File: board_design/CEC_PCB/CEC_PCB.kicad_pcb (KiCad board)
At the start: 4 copper layers, 4 parts, among them J1 HDMI_A, J2 HDMI_A, J3 Conn_01x12_Socket, J4 Conn_01x12_Socket

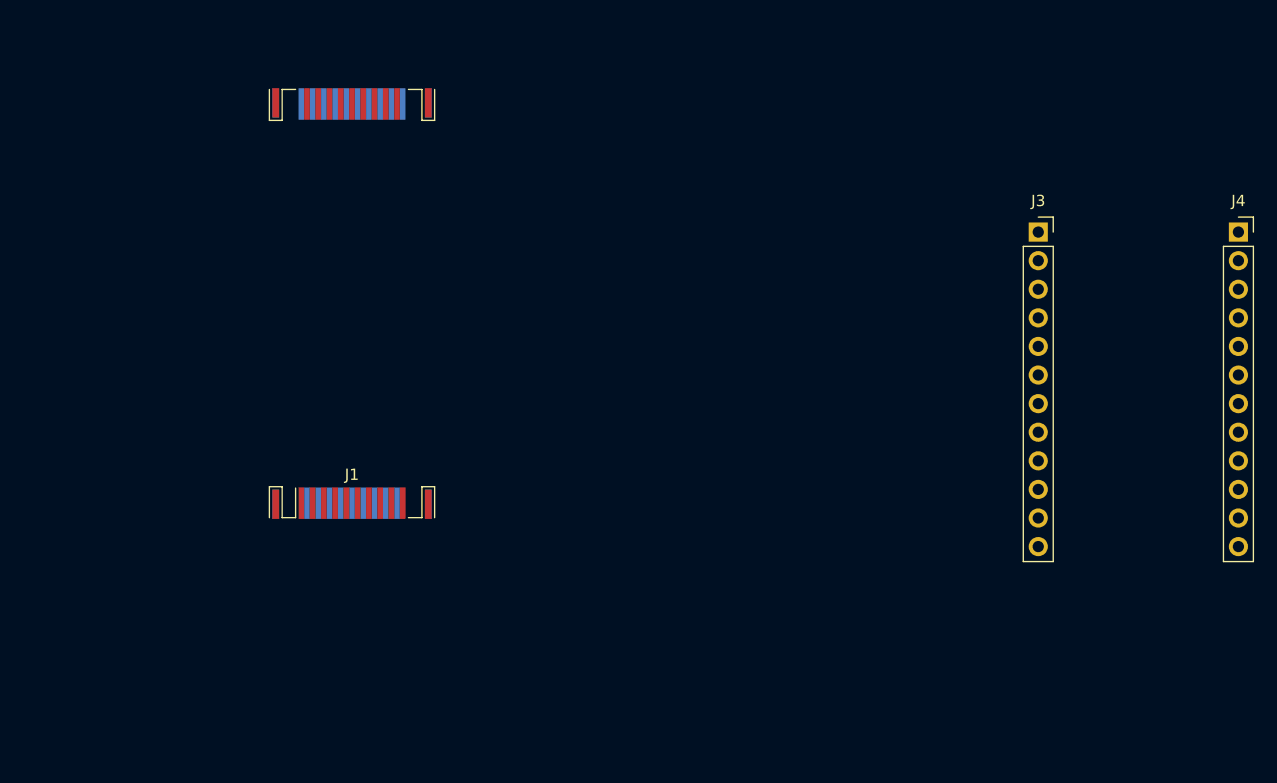
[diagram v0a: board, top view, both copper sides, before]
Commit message: Broke out Pro Micro pins using a connector with two rows Level shifter between CEC pins Mounting holes and debug pins PCB outline defined Crude component placement Copper pours on GND planes
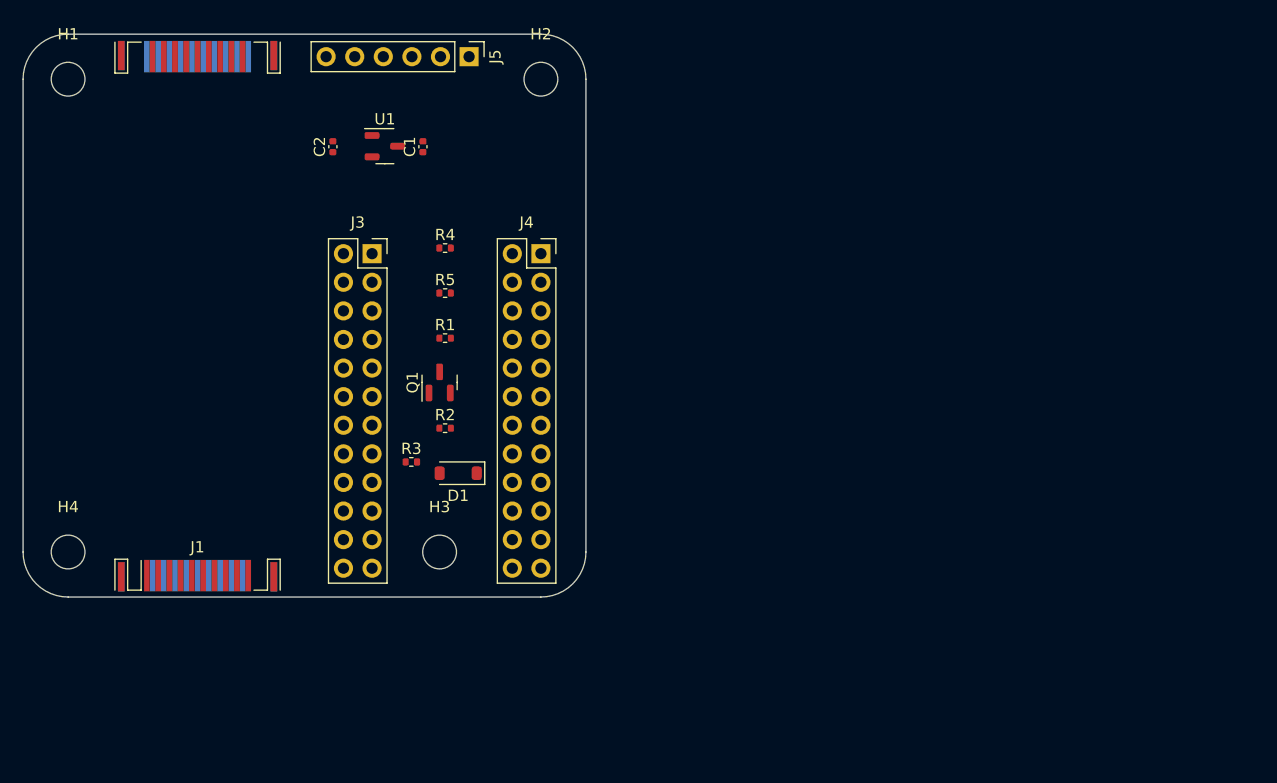
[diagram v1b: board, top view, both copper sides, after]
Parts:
- added C1: 0.1u, Capacitor_SMD:C_0402_1005Metric, F.Cu at (115.5, 61.0)
- added C2: 0.1u, Capacitor_SMD:C_0402_1005Metric, F.Cu at (107.5, 61.0)
- added D1: 1N4148W, Diode_SMD:D_SOD-123, F.Cu at (118.7, 90.0)
- added H1: MountingHole, MountingHole:MountingHole_3mm, F.Cu at (84.0, 55.0)
- added H2: MountingHole, MountingHole:MountingHole_3mm, F.Cu at (126.0, 55.0)
- added H3: MountingHole, MountingHole:MountingHole_3mm, F.Cu at (117.0, 97.0)
- added H4: MountingHole, MountingHole:MountingHole_3mm, F.Cu at (84.0, 97.0)
- added J5: Conn_01x06_Pin, Connector_PinHeader_2.54mm:PinHeader_1x06_P2.54mm_Vertical, F.Cu at (119.6, 53.0)
- added Q1: BSS138, Package_TO_SOT_SMD:SOT-23, F.Cu at (117.0, 81.9)
- added R1: 10k, Resistor_SMD:R_0402_1005Metric, F.Cu at (117.5, 78.0)
- added R2: 10k, Resistor_SMD:R_0402_1005Metric, F.Cu at (117.5, 86.0)
- added R3: 27k, Resistor_SMD:R_0402_1005Metric, F.Cu at (114.5, 89.0)
- added R4: 2k2, Resistor_SMD:R_0402_1005Metric, F.Cu at (117.5, 70.0)
- added R5: 2k2, Resistor_SMD:R_0402_1005Metric, F.Cu at (117.5, 74.0)
- added U1: XC6206PxxxMR, Package_TO_SOT_SMD:SOT-23-3, F.Cu at (112.1, 61.0)
- J3, J4: value Conn_01x12_Socket -> Conn_02x12_Odd_Even; footprint Connector_PinSocket_2.54mm:PinSocket_1x12_P2.54mm_Vertical -> Connector_PinSocket_2.54mm:PinSocket_2x12_P2.54mm_Vertical
- moved J4 62.0 mm to (126.0, 70.5)
- moved J3 59.2 mm to (111.0, 70.5)
- moved J1 15.2 mm to (95.5, 99.1)
- moved J2 14.3 mm to (95.5, 53.0)
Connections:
- J3 pad 1: unconnected-(J3-Pin_1-Pad1) -> /TX
- J3 pad 10: unconnected-(J3-Pin_10-Pad10) -> /SDA
- J3 pad 11: unconnected-(J3-Pin_11-Pad11) -> /SCL
- J3 pad 12: unconnected-(J3-Pin_12-Pad12) -> /SCL
- J3 pad 2: unconnected-(J3-Pin_2-Pad2) -> /TX
- J3 pad 3: unconnected-(J3-Pin_3-Pad3) -> /RX
- J3 pad 4: unconnected-(J3-Pin_4-Pad4) -> /RX
- J3 pad 5: unconnected-(J3-Pin_5-Pad5) -> Net-(J3-Pin_5)
- J3 pad 6: unconnected-(J3-Pin_6-Pad6) -> Net-(J3-Pin_5)
- J3 pad 7: unconnected-(J3-Pin_7-Pad7) -> Net-(J3-Pin_7)
- J3 pad 8: unconnected-(J3-Pin_8-Pad8) -> Net-(J3-Pin_7)
- J3 pad 9: unconnected-(J3-Pin_9-Pad9) -> /SDA
- J4 pad 1: unconnected-(J4-Pin_1-Pad1) -> Net-(J4-Pin_1)
- J4 pad 10: unconnected-(J4-Pin_10-Pad10) -> Net-(J4-Pin_10)
- J4 pad 11: unconnected-(J4-Pin_11-Pad11) -> Net-(J4-Pin_11)
- J4 pad 12: unconnected-(J4-Pin_12-Pad12) -> Net-(J4-Pin_11)
- J4 pad 2: unconnected-(J4-Pin_2-Pad2) -> Net-(J4-Pin_1)
- J4 pad 3: unconnected-(J4-Pin_3-Pad3) -> GND
- J4 pad 4: unconnected-(J4-Pin_4-Pad4) -> GND
- J4 pad 5: unconnected-(J4-Pin_5-Pad5) -> Net-(J4-Pin_5)
- J4 pad 6: unconnected-(J4-Pin_6-Pad6) -> Net-(J4-Pin_5)
- J4 pad 7: unconnected-(J4-Pin_7-Pad7) -> VCC
- J4 pad 8: unconnected-(J4-Pin_8-Pad8) -> VCC
- J4 pad 9: unconnected-(J4-Pin_9-Pad9) -> Net-(J4-Pin_10)
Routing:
- added copper zone on In1.Cu, net GND
- added copper zone on In2.Cu, net GND
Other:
- board outline added: 50 x 50 mm

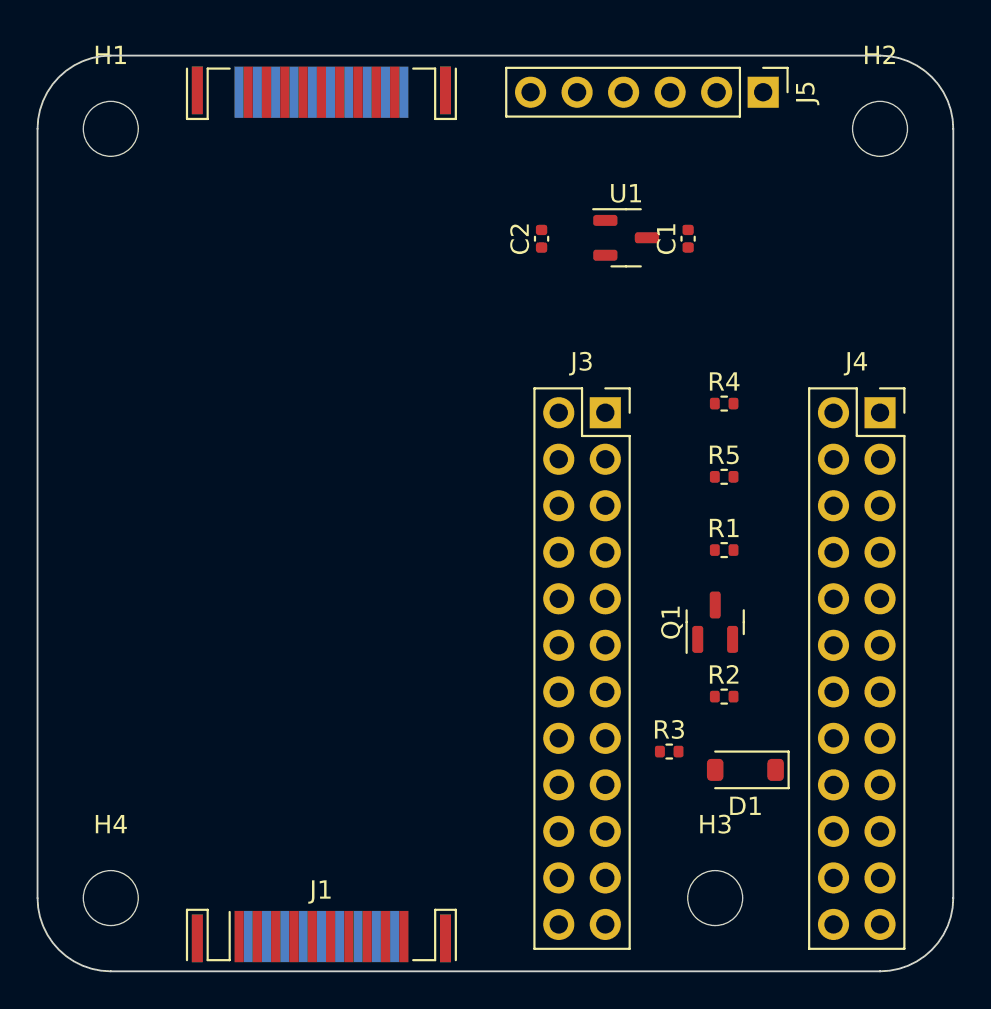
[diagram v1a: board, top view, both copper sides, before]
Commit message: Labels for nets in the schematic Board size change Parts placement change Basic routing
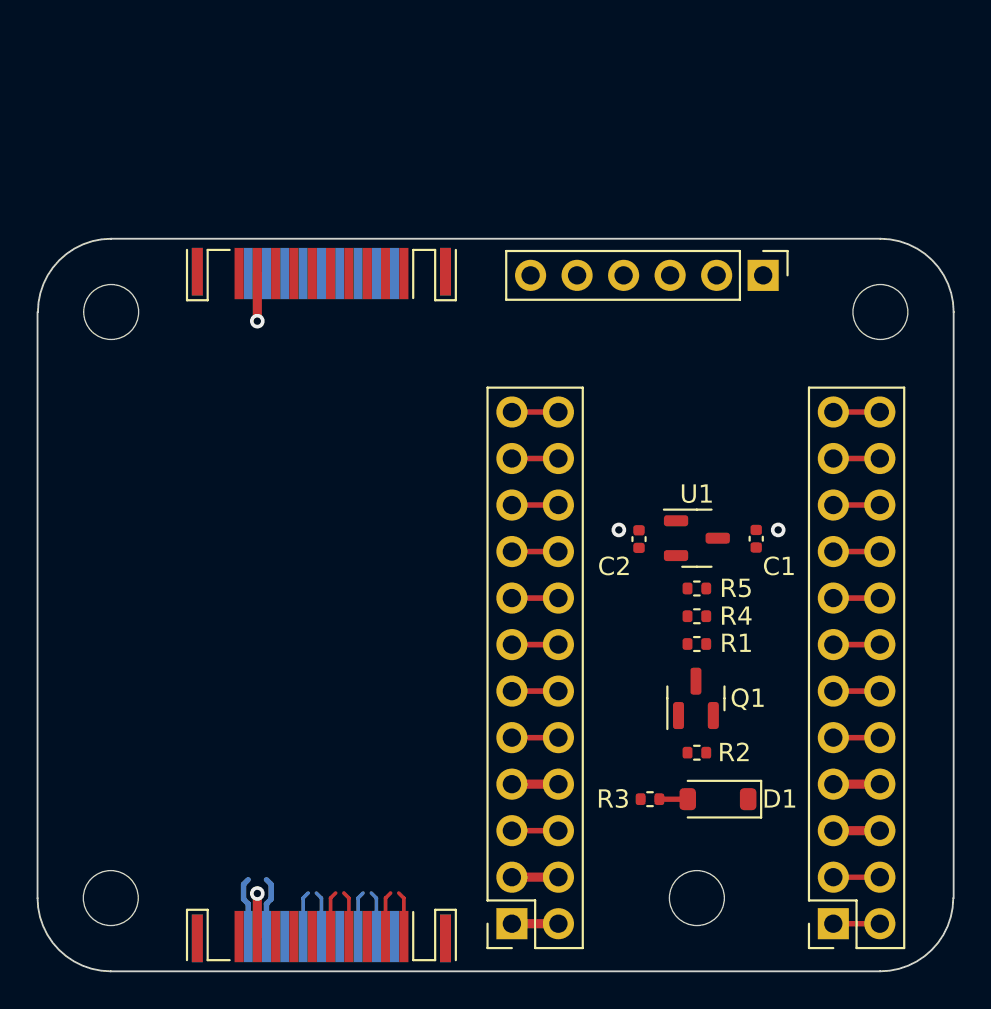
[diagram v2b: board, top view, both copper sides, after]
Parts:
- J2: moved to F.Cu
- moved J4 34.4 mm to (105.9, 98.4), turned to 180 degrees
- moved J3 30.6 mm to (123.5, 98.4), turned to 180 degrees
- moved C2 17.2 mm to (112.8, 77.4)
- moved U1 16.8 mm to (116.0, 77.3)
- moved C1 16.8 mm to (119.2, 77.4)
- moved R4 11.7 mm to (116.0, 81.6), turned to 180 degrees
- moved H1 10.0 mm to (84.0, 65.0)
- moved H2 10.0 mm to (126.0, 65.0)
- moved J5 10.0 mm to (119.6, 63.0)
- moved J2 9.90 mm to (95.5, 62.9), turned to 180 degrees
- moved R5 6.28 mm to (116.0, 80.1), turned to 180 degrees
- moved R1 5.34 mm to (116.0, 83.1)
- moved Q1 4.29 mm to (115.9, 86.1)
- moved R2 3.41 mm to (116.0, 89.1)
- moved R3 2.80 mm to (113.4, 91.6)
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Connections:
- net Net-(D1-A) renamed /D_K
- net Net-(J1-+5V) renamed /+5V
- net Net-(J1-CK+) renamed /CK+
- net Net-(J1-CK-) renamed /CK-
- net Net-(J1-D0+) renamed /D0+
- net Net-(J1-D0-) renamed /D0-
- net Net-(J1-D1+) renamed /D1+
- net Net-(J1-D1-) renamed /D1-
- net Net-(J1-D2+) renamed /D2+
- net Net-(J1-D2-) renamed /D2-
- net Net-(J1-HPD) renamed /HPD
- net Net-(J1-UTILITY) renamed /UTILITY
- net Net-(J3-Pin_13) renamed /PD4
- net Net-(J3-Pin_15) renamed /PC6
- net Net-(J3-Pin_17) renamed /PD7
- net Net-(J3-Pin_21) renamed /PB4
- net Net-(J3-Pin_23) renamed /PB5
- net Net-(J4-Pin_1) renamed /RAW
- net Net-(J4-Pin_10) renamed /PF4
- net Net-(J4-Pin_11) renamed /PF5
- net Net-(J4-Pin_13) renamed /PF6
- net Net-(J4-Pin_15) renamed /PF7
- net Net-(J4-Pin_17) renamed /PB1
- net Net-(J4-Pin_19) renamed /PB3
- net Net-(J4-Pin_21) renamed /PB2
- net Net-(J4-Pin_23) renamed /PB6
- net Net-(J4-Pin_5) renamed /RES
- J1 pad 11: unconnected-(J1-CKS-Pad11) -> /CKS
- J1 pad 2: unconnected-(J1-D2S-Pad2) -> /D2S
- J1 pad 5: unconnected-(J1-D1S-Pad5) -> /D1S
- J1 pad 8: unconnected-(J1-D0S-Pad8) -> /D0S
- J2 pad 11: unconnected-(J2-CKS-Pad11) -> /CKS
- J2 pad 2: unconnected-(J2-D2S-Pad2) -> /D2S
- J2 pad 5: unconnected-(J2-D1S-Pad5) -> /D1S
- J2 pad 8: unconnected-(J2-D0S-Pad8) -> /D0S
- J3 pad 5: Net-(J3-Pin_5) -> GND
- J3 pad 6: Net-(J3-Pin_5) -> GND
- J3 pad 7: Net-(J3-Pin_7) -> GND
- J3 pad 8: Net-(J3-Pin_7) -> GND
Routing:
- net GND: track 0.00 -> 12.6 mm, vias 0 -> 4
- net /SDA: track 0.00 -> 5.85 mm
- net /+5V: track 0.00 -> 3.31 mm
- net /PF4: track 0.00 -> 2.57 mm
- net VCC: track 0.00 -> 2.54 mm
- net /TX: track 0.00 -> 2.54 mm
- net /SCL: track 0.00 -> 2.54 mm
- net /RX: track 0.00 -> 2.54 mm
- net /RES: track 0.00 -> 2.54 mm
- net /RAW: track 0.00 -> 2.54 mm
- net /PF7: track 0.00 -> 2.54 mm
- net /PF6: track 0.00 -> 2.54 mm
- net /PF5: track 0.00 -> 2.54 mm
- net /PD7: track 0.00 -> 2.54 mm
- net /PD4: track 0.00 -> 2.54 mm
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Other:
- board size 50 x 50 mm -> 50 x 40 mm

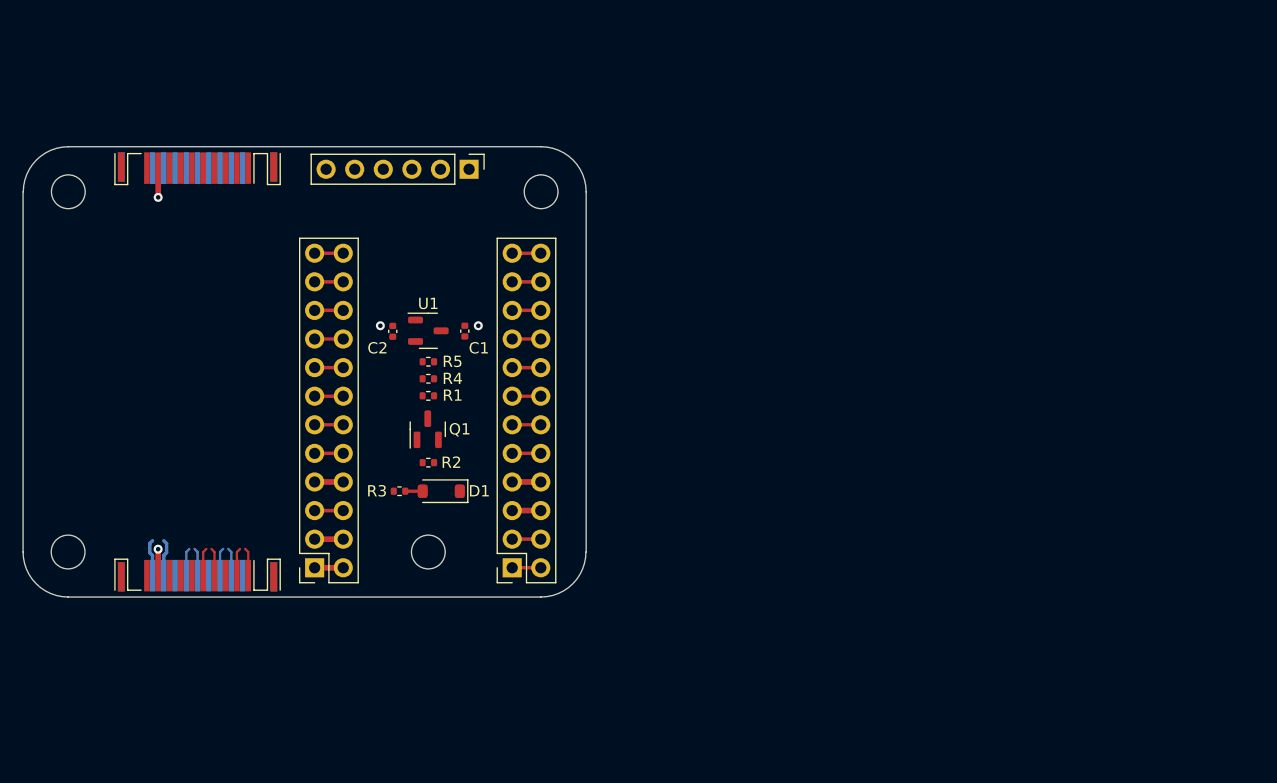
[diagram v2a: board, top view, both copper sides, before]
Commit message: Track routing done
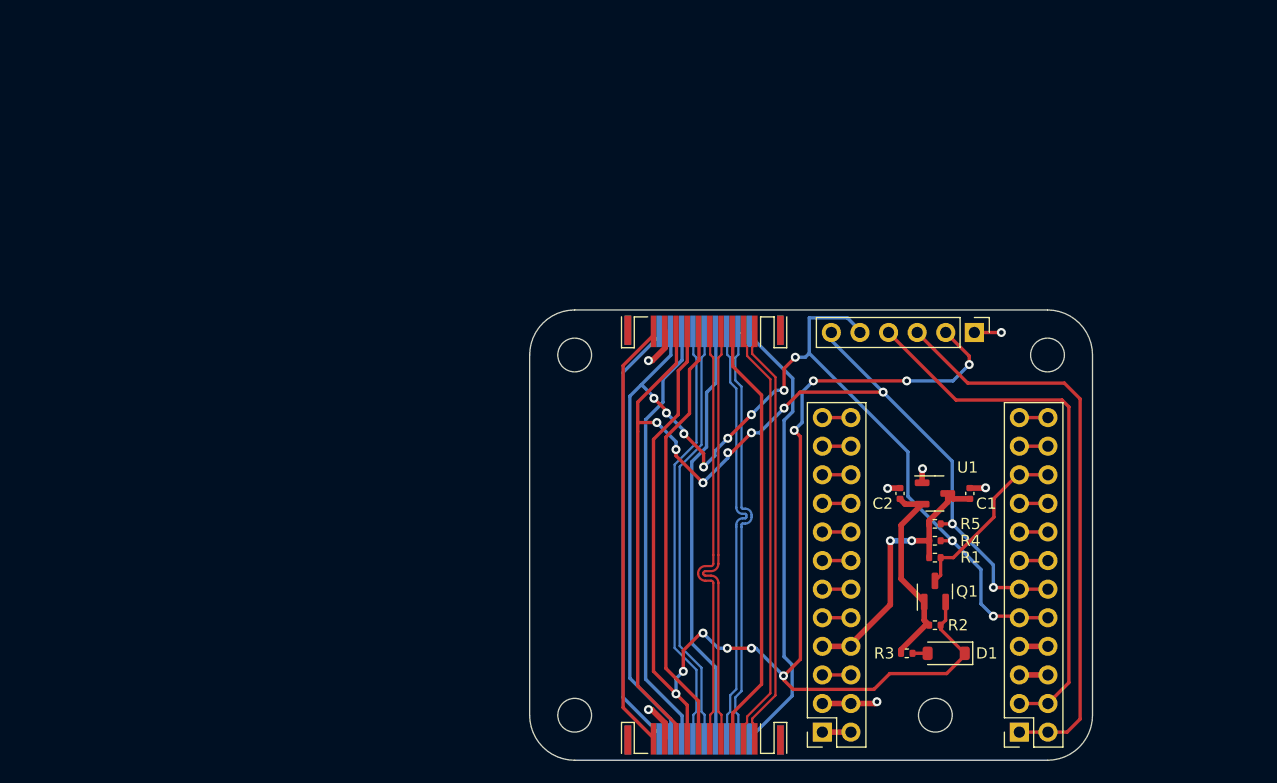
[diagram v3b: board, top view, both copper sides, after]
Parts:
- moved J4 47.4 mm to (151.0, 113.0)
- moved J3 47.4 mm to (168.5, 113.0)
- moved H3 47.3 mm to (161.0, 111.5)
- moved C2 47.3 mm to (157.9, 91.8)
- moved R3 47.3 mm to (158.5, 106.0)
- moved Q1 47.3 mm to (161.0, 100.5)
- moved H4 47.3 mm to (129.0, 111.5)
- moved J1 47.3 mm to (140.5, 113.6)
- moved J2 47.3 mm to (140.5, 77.4)
- moved U1 47.3 mm to (161.0, 91.8)
- moved H1 47.3 mm to (129.0, 79.5)
- moved H2 47.3 mm to (171.0, 79.5)
- moved R2 47.3 mm to (161.0, 103.5)
- moved R5 47.2 mm to (161.0, 94.5)
- moved R4 47.2 mm to (161.0, 96.0)
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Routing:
- net /CEC: track 0.00 -> 124.3 mm, vias 0 -> 10
- net /SDA: track 5.85 -> 108.8 mm, vias 0 -> 10
- net /SCL: track 2.54 -> 102.8 mm, vias 0 -> 9
- net /TX: track 2.54 -> 51.2 mm
- net /RX: track 2.54 -> 48.4 mm
- net /D2S: track 0.00 -> 40.0 mm
- net /UTILITY: track 0.00 -> 38.9 mm
- net /CKS: track 0.00 -> 38.6 mm
- net /HPD: track 0.00 -> 38.5 mm
- net /D1S: track 0.00 -> 38.3 mm
- net /D0S: track 0.00 -> 38.0 mm
- net /D1+: track 2.49 -> 38.4 mm
- net /D0+: track 2.49 -> 38.3 mm
- net /D0-: track 2.49 -> 38.3 mm
- net /D2-: track 2.49 -> 38.1 mm
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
